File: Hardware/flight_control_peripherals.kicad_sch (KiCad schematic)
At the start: 16 parts, among them J10 Conn_01x06, J2 Conn_02x10_Odd_Even, J3 Conn_01x10, J4 Conn_01x04, J5 Conn_01x04, J6 Conn_01x04, J8 Conn_01x04, J9 Conn_01x04, U13 24CW1280T-I/OT, U14 W25N01GVZEIG_TR, U17 PCA9685PW_118

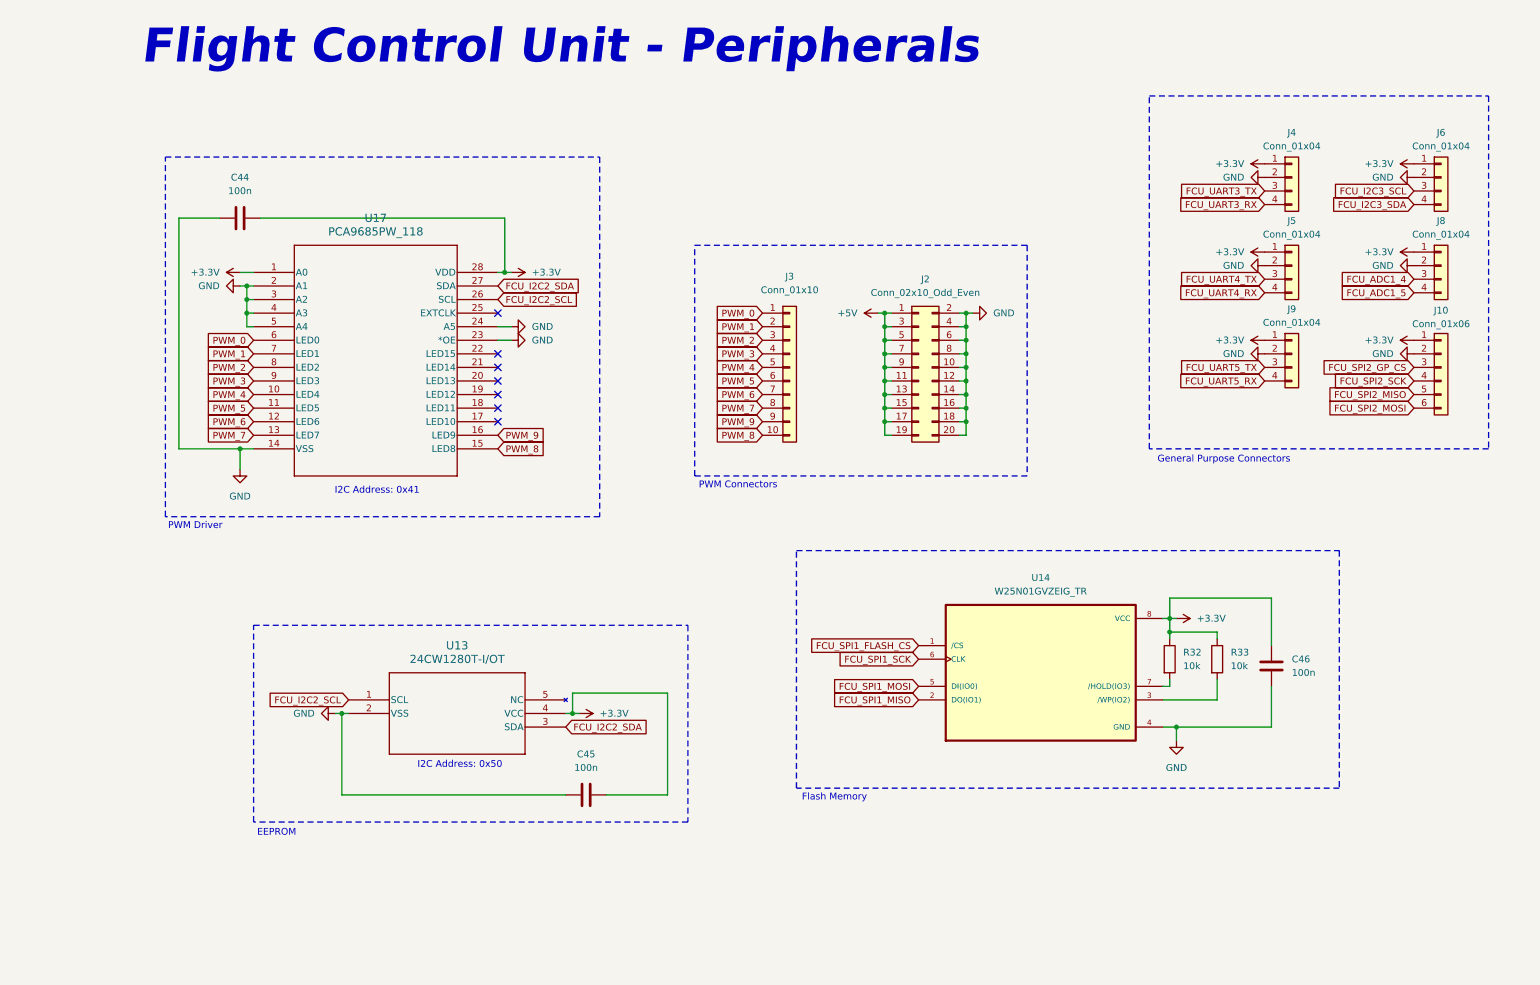
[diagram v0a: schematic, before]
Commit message: fcu, nu schematics, problem with pins
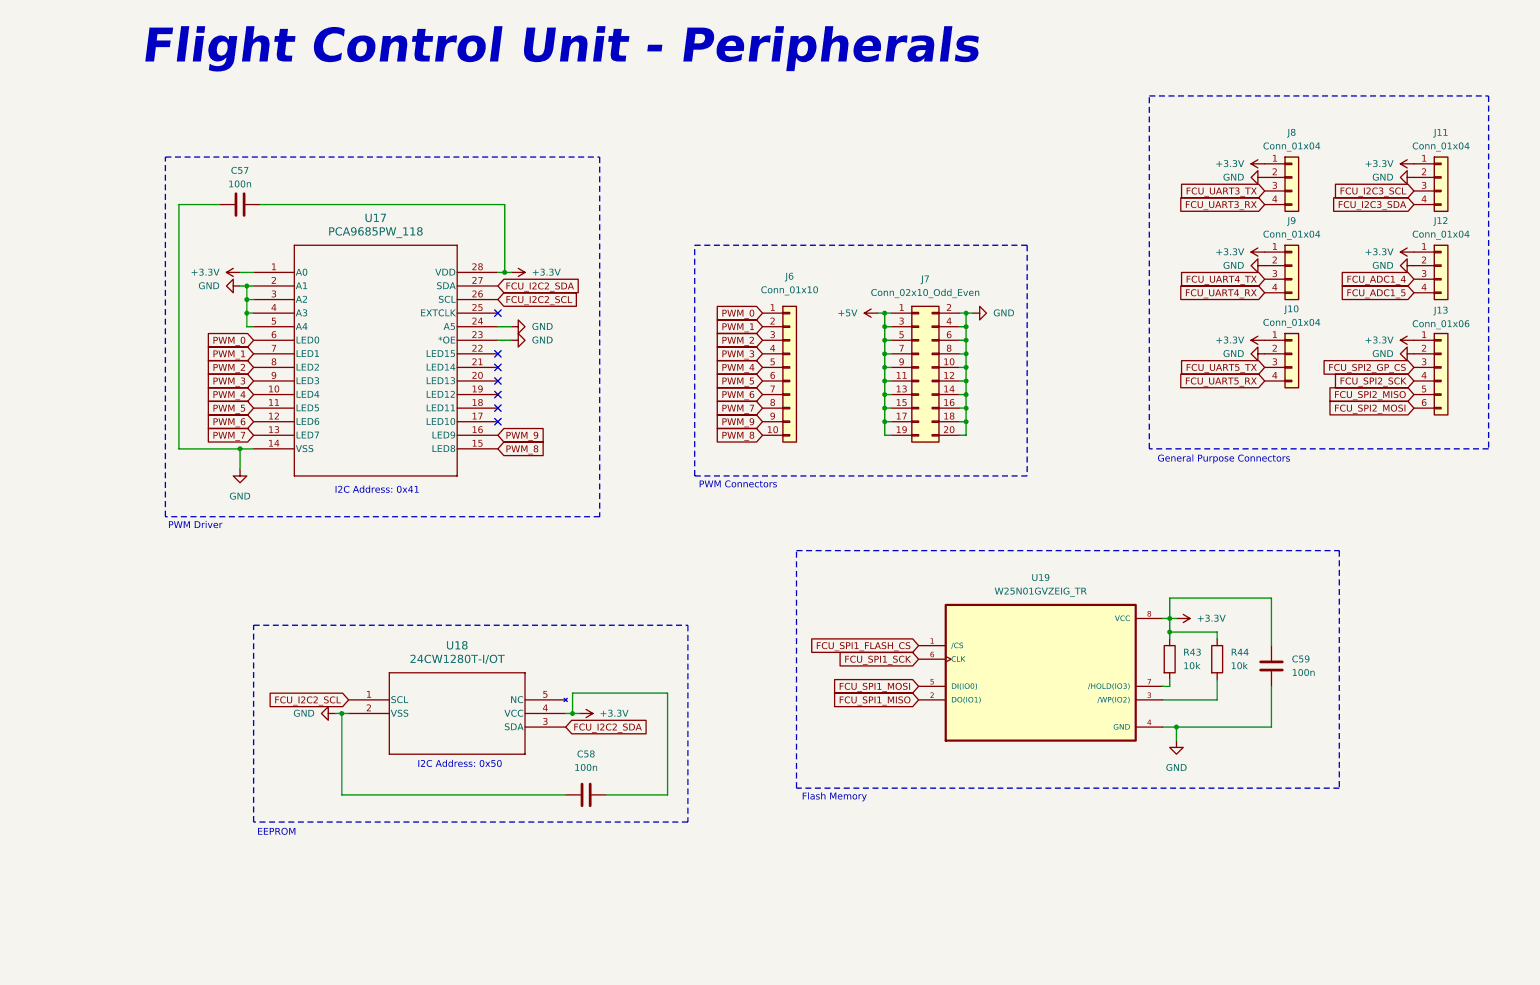
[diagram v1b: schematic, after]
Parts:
- renumbered C44 to C57, C45 to C58, C46 to C59, J9 to J10, J6 to J11, J8 to J12, J10 to J13, J3 to J6, J2 to J7, J4 to J8, J5 to J9, R32 to R43, R33 to R44, U13 to U18, U14 to U19
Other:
- company: (none) -> Breno Soares Alves
- title: (none) -> Flight Control Unit - Peripherals
- moved on the sheet: C57

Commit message: added projects, schematic almost done, need revision
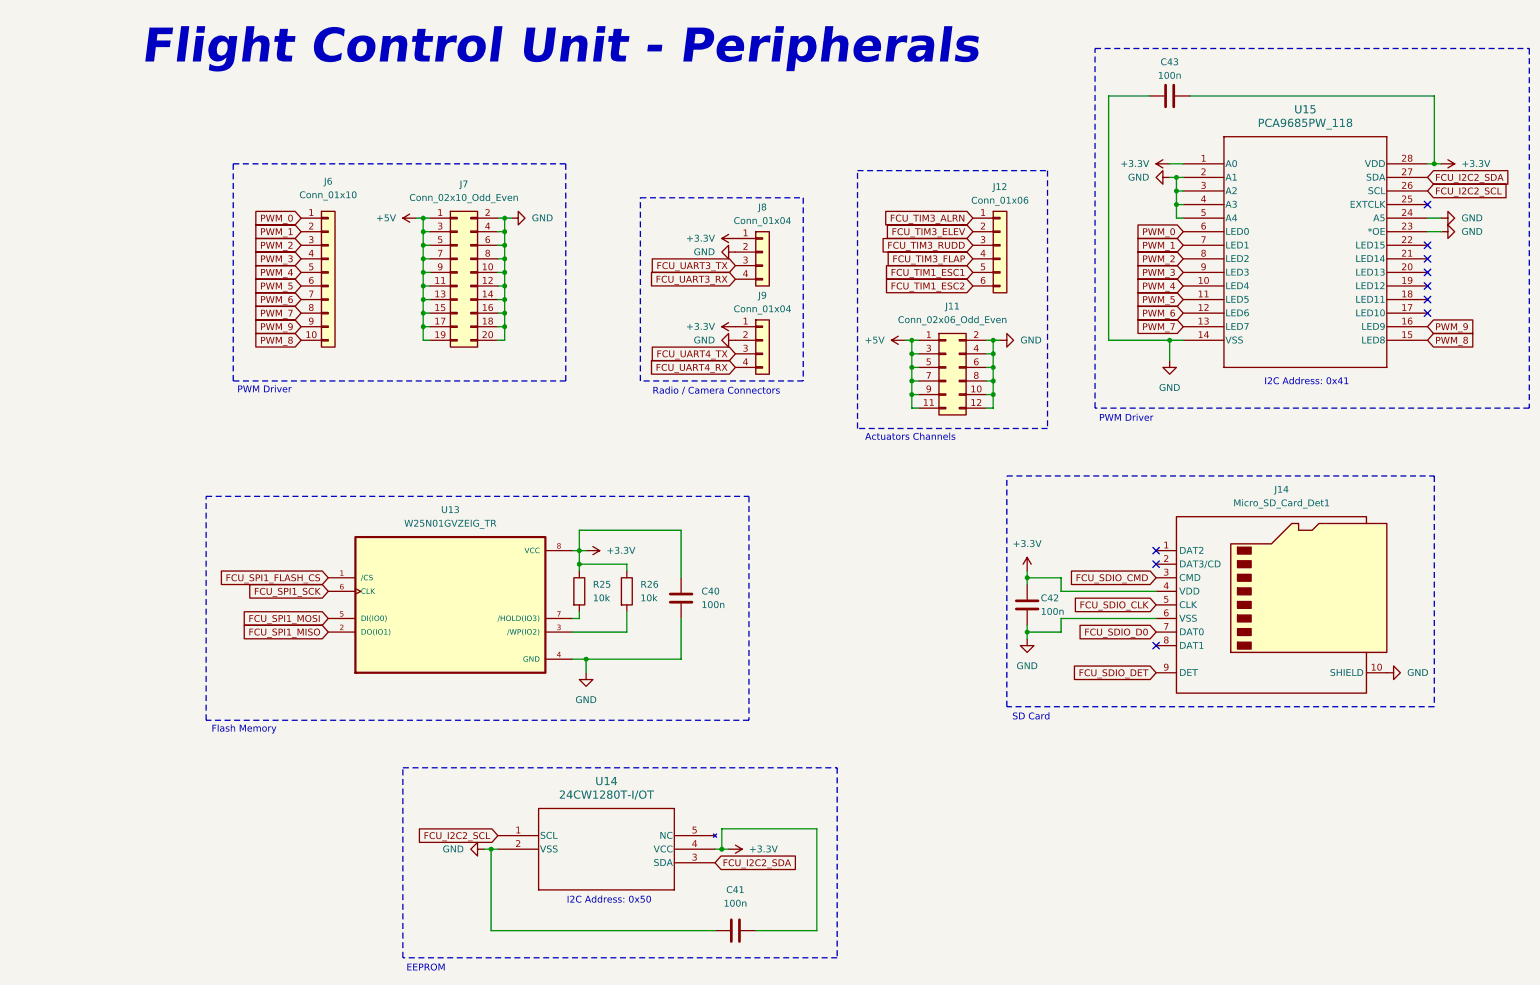
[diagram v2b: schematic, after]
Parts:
- removed J10, J11, J12: Conn_01x04, symbol Connector_Generic:Conn_01x04
- removed J13: Conn_01x06, symbol Connector_Generic:Conn_01x06
- added C42: 100n, symbol Device:C
- added J11: Conn_02x06_Odd_Even, symbol Connector_Generic:Conn_02x06_Odd_Even
- added J12: Conn_01x06, symbol Connector_Generic:Conn_01x06
- added J14: Micro_SD_Card_Det1, symbol Connector:Micro_SD_Card_Det1
- renumbered C59 to C40, C58 to C41, C57 to C43, R43 to R25, R44 to R26, U19 to U13, U18 to U14, U17 to U15
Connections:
- net +3.3V: now also C42.1, J14.4 (VDD)
- net +5V: now also J11.1 (Pin_1), J11.11 (Pin_11), J11.3 (Pin_3), J11.5 (Pin_5), J11.7 (Pin_7), J11.9 (Pin_9)
- net GND: now also C42.2, J11.10 (Pin_10), J11.12 (Pin_12), J11.2 (Pin_2), J11.4 (Pin_4), J11.6 (Pin_6), J11.8 (Pin_8), J14.10 (SHIELD), J14.6 (VSS)
- new net FCU_SDIO_CLK: J14.5 (CLK)
- new net FCU_SDIO_CMD: J14.3 (CMD)
- new net FCU_SDIO_D0: J14.7 (DAT0)
- new net FCU_SDIO_DET: J14.9 (DET)
- new net FCU_TIM1_ESC1: J12.5 (Pin_5)
- new net FCU_TIM1_ESC2: J12.6 (Pin_6)
- new net FCU_TIM3_ALRN: J12.1 (Pin_1)
- new net FCU_TIM3_ELEV: J12.2 (Pin_2)
- new net FCU_TIM3_FLAP: J12.4 (Pin_4)
- new net FCU_TIM3_RUDD: J12.3 (Pin_3)
- no-connect marks 7 -> 10
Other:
- note added: "Actuators Channels"
- note added: "Radio / Camera Connectors"
- note added: "SD Card"
- note removed: "General Purpose Connectors"
- note removed: "PWM Connectors"
- moved on the sheet: C40, C41, C43, J6, J7, J8, J9, R25, R26, U13, U14, U15

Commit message: sd card receptacle 10u capacitor
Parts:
- added C59: 10u, symbol Device:C_Polarized
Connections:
- net +3.3V: now also C59.1
- net GND: now also C59.2
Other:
- moved on the sheet: C42
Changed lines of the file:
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@@
 	)
 	(rectangle
-		(start 179.07 100.33)
+		(start 167.64 100.33)
 		(end 259.08 143.51)
 		(stroke
@@
 	(text "SD Card"
 		(exclude_from_sim no)
-		(at 183.642 145.542 0)
+		(at 172.212 145.542 0)
 		(effects
 			(font
@@
 	)
 	(junction
-		(at 182.88 119.38)
+		(at 171.45 119.38)
 		(diameter 0)
 		(color 0 0 0 0)
@@
 	)
 	(junction
-		(at 182.88 129.54)
+		(at 171.45 129.54)
 		(diameter 0)
 		(color 0 0 0 0)
@@
 	)
 	(junction
+		(at 181.61 119.38)
+		(diameter 0)
+		(color 0 0 0 0)
+	)
+	(junction
 		(at 209.55 74.93)
 		(diameter 0)
@@
 	)
 	(junction
+		(at 181.61 129.54)
+		(diameter 0)
+		(color 0 0 0 0)
+	)
+	(junction
 		(at 176.53 77.47)
 		(diameter 0)
@@
 	(wire
 		(pts
-			(xy 182.88 118.11) (xy 182.88 119.38)
+			(xy 171.45 118.11) (xy 171.45 119.38)
 		)
 		(stroke
@@
 	(wire
 		(pts
-			(xy 182.88 119.38) (xy 182.88 120.65)
+			(xy 171.45 119.38) (xy 171.45 120.65)
 		)
 		(stroke
@@
 	(wire
 		(pts
-			(xy 182.88 129.54) (xy 182.88 130.81)
+			(xy 171.45 129.54) (xy 171.45 130.81)
 		)
 		(stroke
@@
 	(wire
 		(pts
-			(xy 182.88 129.54) (xy 189.23 129.54)
+			(xy 171.45 129.54) (xy 181.61 129.54)
 		)
 		(stroke
@@
 	(wire
 		(pts
+			(xy 181.61 119.38) (xy 189.23 119.38)
+		)
+		(stroke
+			(width 0)
+			(type default)
+		)
+	)
+	(wire
+		(pts
 			(xy 213.36 29.21) (xy 259.08 29.21)
 		)
@@
 	(wire
 		(pts
+			(xy 181.61 128.27) (xy 181.61 129.54)
+		)
+		(stroke
+			(width 0)
+			(type default)
+		)
+	)
+	(wire
+		(pts
 			(xy 176.53 77.47) (xy 175.26 77.47)
 		)
@@
 	(wire
 		(pts
+			(xy 181.61 129.54) (xy 189.23 129.54)
+		)
+		(stroke
+			(width 0)
+			(type default)
+		)
+	)
+	(wire
+		(pts
 			(xy 69.85 64.77) (xy 69.85 67.31)
 		)
@@
 	(wire
 		(pts
-			(xy 182.88 128.27) (xy 182.88 129.54)
+			(xy 171.45 128.27) (xy 171.45 129.54)
 		)
 		(stroke
@@
 	(wire
 		(pts
+			(xy 181.61 119.38) (xy 181.61 120.65)
+		)
+		(stroke
+			(width 0)
+			(type default)
+		)
+	)
+	(wire
+		(pts
 			(xy 209.55 74.93) (xy 198.12 74.93)
 		)
@@
 	(wire
 		(pts
-			(xy 182.88 119.38) (xy 189.23 119.38)
+			(xy 171.45 119.38) (xy 181.61 119.38)
 		)
 		(stroke
@@
 	)
 	(symbol
+		(lib_id "Device:C_Polarized")
+		(at 181.61 124.46 0)
+		(unit 1)
+		(exclude_from_sim no)
+		(in_bom yes)
+		(on_board yes)
+		(dnp no)
+		(property "Reference" "C59"
+			(at 184.404 123.19 0)
+			(effects
+				(font
+					(size 1.27 1.27)
+				)
+				(justify left)
+			)
+		)
+		(property "Value" "10u"
+			(at 184.404 125.73 0)
+			(effects
+				(font
+					(size 1.27 1.27)
+				)
+				(justify left)
+			)
+		)
+		(property "Footprint" ""
+			(at 182.5752 128.27 0)
+			(effects
+				(font
+					(size 1.27 1.27)
+				)
+				(hide yes)
+			)
+		)
+		(property "Datasheet" "~"
+			(at 181.61 124.46 0)
+			(effects
+				(font
+					(size 1.27 1.27)
+				)
+				(hide yes)
+			)
+		)
+		(property "Description" "Polarized capacitor"
+			(at 181.61 124.46 0)
+			(effects
+				(font
+					(size 1.27 1.27)
+				)
+				(hide yes)
+			)
+		)
+		(pin "1"
+		)
+		(pin "2"
+		)
+		(instances
+			(project ""
+				(path "/8dc22ddc-eb0a-4b80-a714-26a959e826d2/2b3e482d-66cf-439d-9529-121b0ac868e2"
+					(reference "C59")
+					(unit 1)
+				)
+			)
+		)
+	)
+	(symbol
 		(lib_id "power:+3.3V")
-		(at 182.88 118.11 0)
+		(at 171.45 118.11 0)
 		(unit 1)
 		(exclude_from_sim no)
@@
 		(fields_autoplaced yes)
 		(property "Reference" "#PWR085"
-			(at 182.88 121.92 0)
+			(at 171.45 121.92 0)
 			(effects
 				(font
@@
 		)
 		(property "Value" "+3.3V"
-			(at 182.88 113.03 0)
+			(at 171.45 113.03 0)
 			(effects
 				(font
@@
 		)
 		(property "Footprint" ""
-			(at 182.88 118.11 0)
+			(at 171.45 118.11 0)
 			(effects
 				(font
@@
 		)
 		(property "Datasheet" ""
-			(at 182.88 118.11 0)
+			(at 171.45 118.11 0)
 			(effects
 				(font
@@
 		)
 		(property "Description" "Power symbol creates a global label with name \"+3.3V\""
-			(at 182.88 118.11 0)
+			(at 171.45 118.11 0)
 			(effects
 				(font
@@
 	(symbol
 		(lib_id "power:GND")
-		(at 182.88 130.81 0)
+		(at 171.45 130.81 0)
 		(unit 1)
 		(exclude_from_sim no)
@@
 		(fields_autoplaced yes)
 		(property "Reference" "#PWR086"
-			(at 182.88 137.16 0)
+			(at 171.45 137.16 0)
 			(effects
 				(font
@@
 		)
 		(property "Value" "GND"
-			(at 182.88 135.89 0)
+			(at 171.45 135.89 0)
 			(effects
 				(font
@@
 		)
 		(property "Footprint" ""
-			(at 182.88 130.81 0)
+			(at 171.45 130.81 0)
 			(effects
 				(font
@@
 		)
 		(property "Datasheet" ""
-			(at 182.88 130.81 0)
+			(at 171.45 130.81 0)
 			(effects
 				(font
@@
 		)
 		(property "Description" "Power symbol creates a global label with name \"GND\" , ground"
-			(at 182.88 130.81 0)
+			(at 171.45 130.81 0)
 			(effects
 				(font
@@
 	(symbol
 		(lib_id "Device:C")
-		(at 182.88 124.46 0)
+		(at 171.45 124.46 0)
 		(unit 1)
 		(exclude_from_sim no)
@@
 		(dnp no)
 		(property "Reference" "C42"
-			(at 185.42 123.19 0)
+			(at 173.99 123.19 0)
 			(effects
 				(font
@@
 		)
 		(property "Value" "100n"
-			(at 185.42 125.73 0)
+			(at 173.99 125.73 0)
 			(effects
 				(font
@@
 		)
 		(property "Footprint" ""
-			(at 183.8452 128.27 0)
+			(at 172.4152 128.27 0)
 			(effects
 				(font
@@
 		)
 		(property "Datasheet" "~"
-			(at 182.88 124.46 0)
+			(at 171.45 124.46 0)
 			(effects
 				(font
@@
 		)
 		(property "Description" "Unpolarized capacitor"
-			(at 182.88 124.46 0)
+			(at 171.45 124.46 0)
 			(effects
 				(font

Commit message: version 0.1.0
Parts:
- renumbered C40 to C55, C41 to C56, C42 to C57, C59 to C58, C43 to C59, J11 to J10, J12 to J11, J14 to J12, R25 to R37, R26 to R38
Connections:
- net +3.3V: no longer J8.1 (Pin_1)
- net +5V: now also J8.1 (Pin_1)
